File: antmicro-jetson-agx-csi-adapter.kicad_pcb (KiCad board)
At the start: 4 copper layers, 73.6 x 41 mm, 106 parts, among them IC1 MAX1708EEE+, J1 QTH-060-03-L-D-A, J2 WE_68715014522_ONE-SIDE, J3 WE_68715014022, J4 BM04B-SRSS-TB-LF-SN, J5 SM06B-SRSS-TB(LF)(SN), J6 SM09B-SRSS-TB(LF)(SN), J7 61300611121, Q1 BSS138AKA, U1 PCA9547BS,118, U2 NTS0102DP

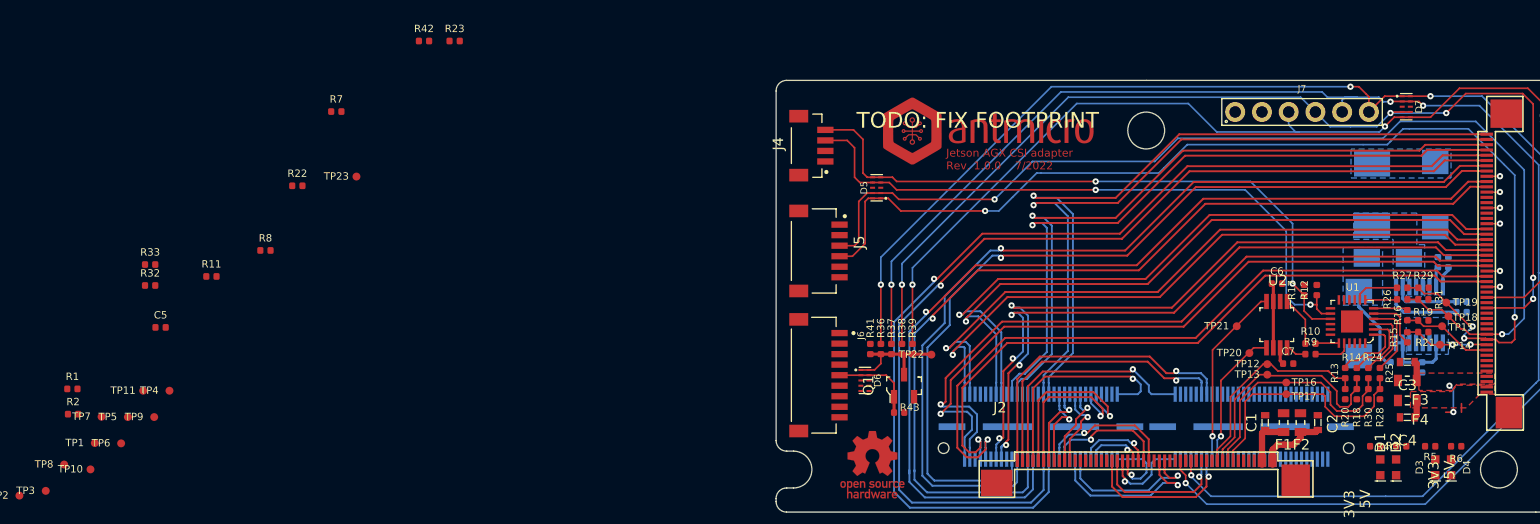
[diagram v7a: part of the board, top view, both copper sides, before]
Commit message: Replaced some components with larger package, routed more signals
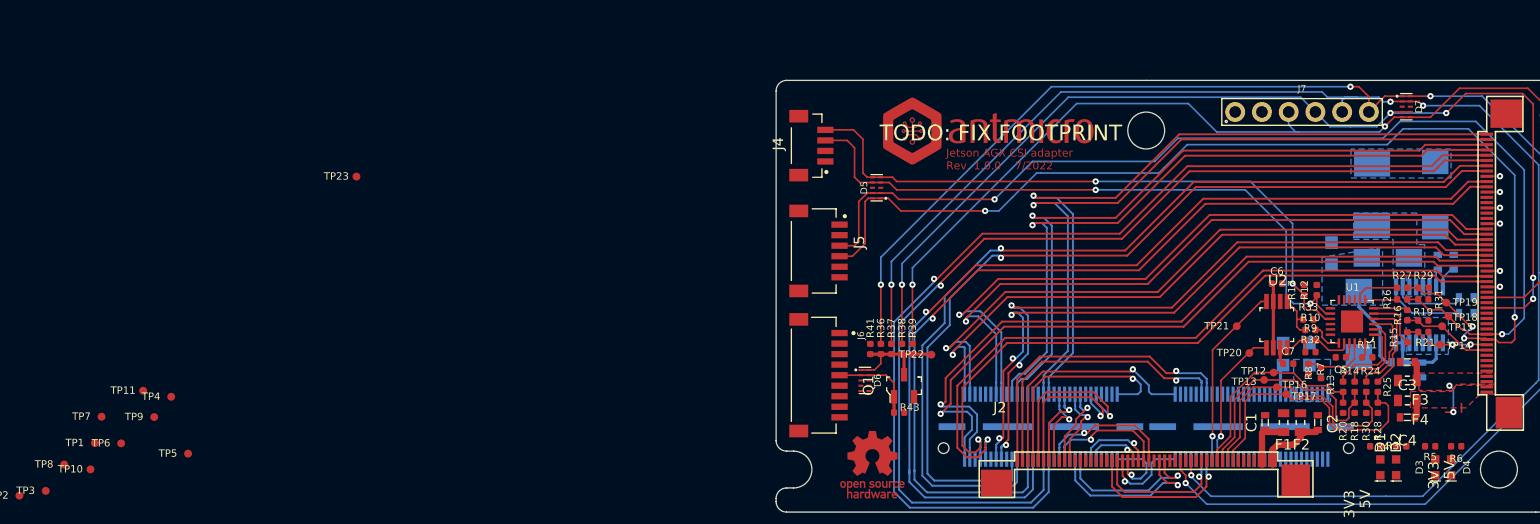
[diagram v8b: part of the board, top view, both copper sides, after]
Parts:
- removed R23: R_2k2_0402, antmicro-footprints:0402-res
- removed R42: R_0R_0402, antmicro-footprints:0402-res
- C10, C11, C9: footprint antmicro-footprints:0402-cap -> antmicro-footprints:0603-cap
- R1, R2: value R_0R_0402 -> R_0R_0805; footprint antmicro-footprints:0402-res -> antmicro-footprints:0805-res; moved to B.Cu
- R22: value R_2k2_0402 -> R_0R_0805; footprint antmicro-footprints:0402-res -> antmicro-footprints:0805-res; moved to B.Cu
- R34, R35, R40: footprint antmicro-footprints:0402-res -> antmicro-footprints:0603-res
- moved R2 117.6 mm to (165.5, 94.0), turned to 90 degrees
- moved R1 115.0 mm to (163.0, 94.0), turned to 90 degrees
- moved C5 112.1 mm to (168.5, 94.3), turned to 180 degrees
- moved R32 110.4 mm to (165.6, 93.8)
- moved R33 110.1 mm to (165.4, 90.7)
- moved R11 110.0 mm to (171.0, 94.3)
- moved R8 100.9 mm to (166.6, 95.8), turned to 90 degrees
- moved R22 98.4 mm to (167.6, 84.5), turned to 90 degrees
- moved R7 95.5 mm to (165.4, 95.4), turned to -90 degrees
- moved TP5 6.69 mm to (59.0, 103.5)
- moved R13 1.32 mm to (168.7, 97.1)
- moved R20 1.32 mm to (168.7, 99.1)
- moved R14 1.32 mm to (169.8, 97.1)
- moved R18 1.32 mm to (169.8, 99.1)
- moved R24 1.32 mm to (170.9, 97.1)
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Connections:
- net Net-(J1-Pad102) renamed /Interface/1V8_CONN
- net Net-(J1-Pad108) renamed /Interface/3V3_CONN
- R22 pad 1: /Auxiliary/MISC_I2C_SDA -> /Auxiliary/5V_C
- R22 pad 2: +3V3 -> +5V
- U1 pad 16: /Auxiliary/MISC_I2C_SDA -> unconnected-(U1-Pad16)
- U1 pad 17: /Auxiliary/MISC_I2C_SCL -> unconnected-(U1-Pad17)
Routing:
- net Net-(R7-Pad1): track 0.00 -> 6.42 mm
- net CAM1_SCL: track 23.4 -> 26.3 mm
- net /Interface/1V8_CONN: track 0.00 -> 2.86 mm
- net Net-(R24-Pad1): track 7.12 -> 8.80 mm
- net +3V3: track 1.61 -> 3.10 mm
- net Net-(R11-Pad1): track 0.00 -> 1.47 mm
- net CAM1_SDA: track 23.4 -> 24.8 mm
- net Net-(R25-Pad1): track 7.37 -> 8.75 mm
- net /Auxiliary/SDA_3V3: track 1.99 -> 3.13 mm
- net Net-(R14-Pad1): track 7.02 -> 8.13 mm
- net Net-(R13-Pad1): track 7.01 -> 8.02 mm
- net Net-(R10-Pad2): track 2.24 -> 3.03 mm
- net Net-(IC1-Pad2): track 6.33 -> 6.98 mm
- net CAM0_SDA: track 20.6 -> 20.0 mm
- added copper zone on B.Cu, net /Interface/3V3_CONN
